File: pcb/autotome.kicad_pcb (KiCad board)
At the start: 2 copper layers, 61 parts, among them SW1 SW_PUSH, SW10 SW_PUSH, SW11 SW_PUSH, SW12 SW_PUSH, SW13 SW_PUSH, SW14 SW_PUSH, SW15 SW_PUSH, SW16 SW_PUSH, SW17 SW_PUSH, SW18 SW_PUSH, SW19 SW_PUSH, SW2 SW_PUSH, SW20 SW_PUSH, SW21 SW_PUSH, SW22 SW_PUSH, SW23 SW_PUSH, SW24 SW_PUSH, SW25 RotaryEncoder_Switch, SW27 SW_PUSH, SW28 SW_PUSH, SW29 SW_PUSH, SW3 SW_PUSH, SW30 SW_PUSH, SW31 SW_SPDT, SW4 SW_PUSH, SW5 SW_PUSH, SW6 SW_PUSH, SW7 SW_PUSH, SW8 SW_PUSH, SW9 SW_PUSH, U1 ProMicro

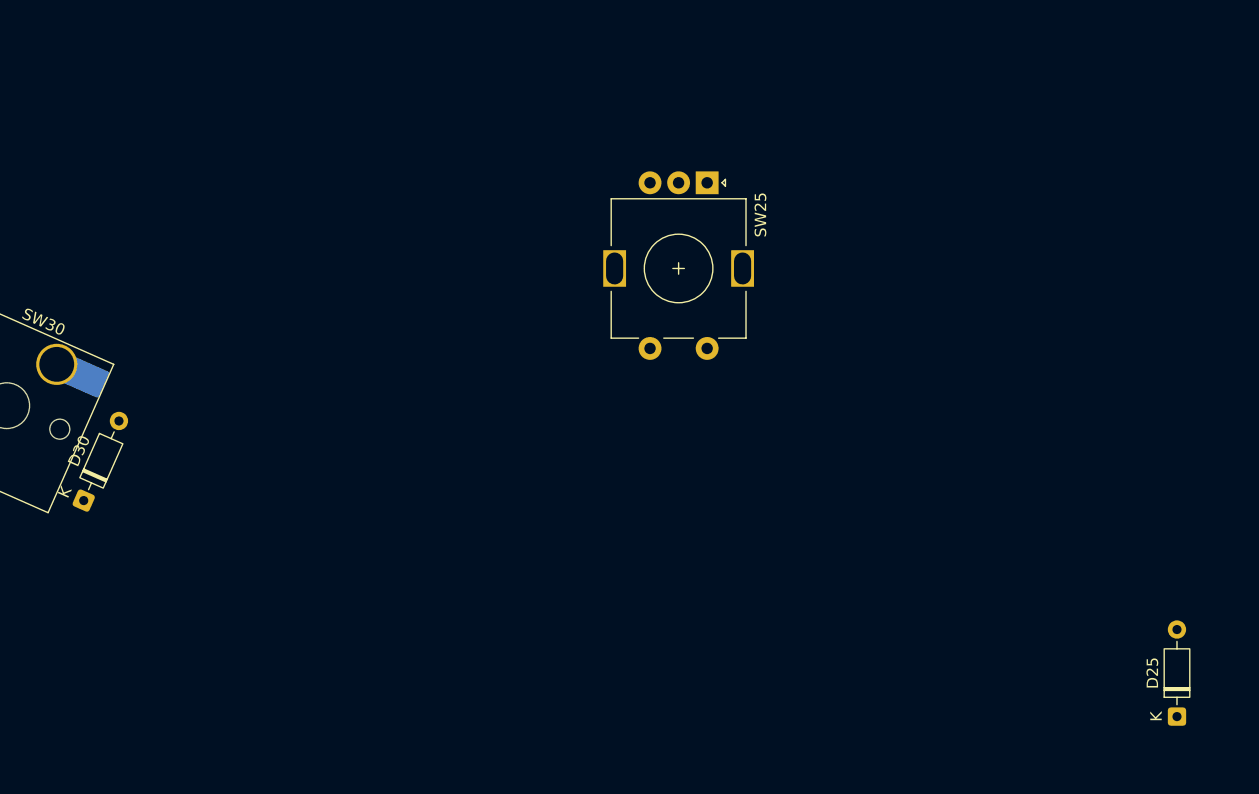
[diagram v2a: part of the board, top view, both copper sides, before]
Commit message: position rotary encoder and diode
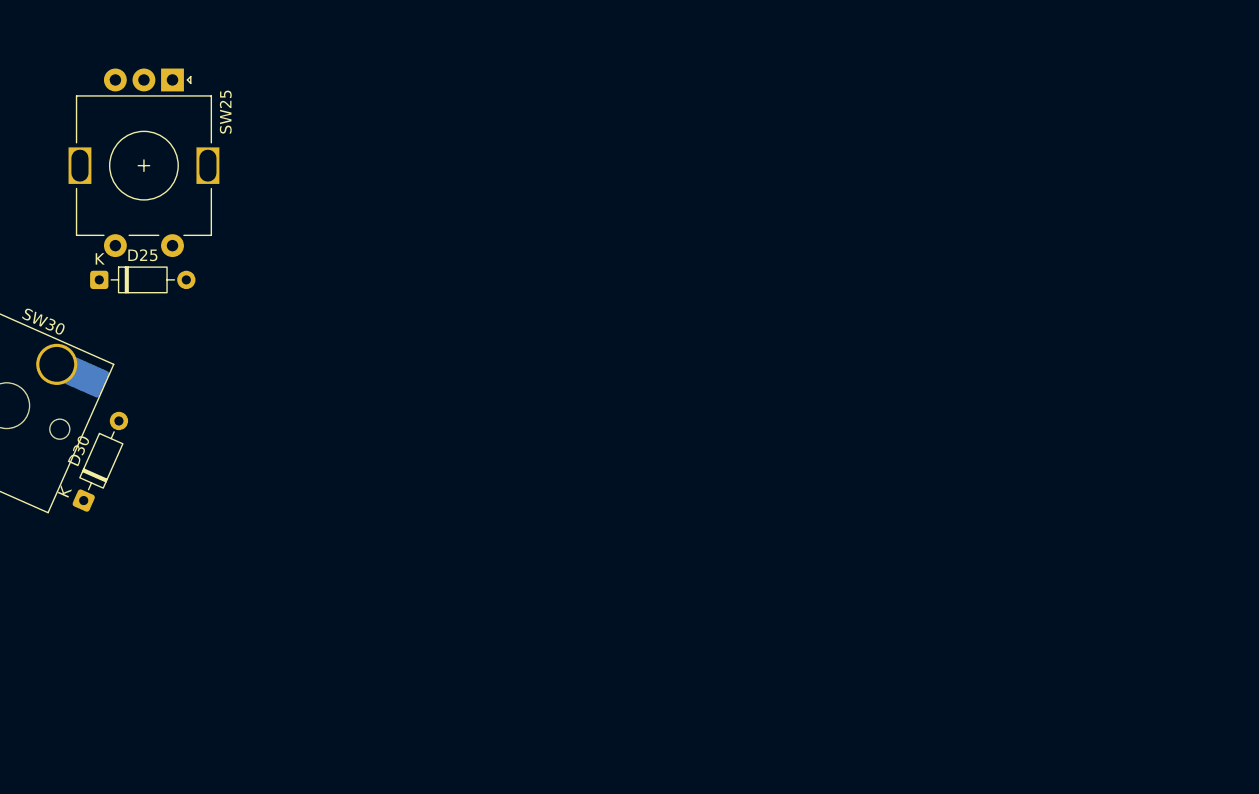
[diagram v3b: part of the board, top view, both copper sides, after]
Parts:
- moved D25 101.8 mm to (143.8, 123.7), turned to 0 degrees
- moved SW25 47.7 mm to (150.2, 106.2)
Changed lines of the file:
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@@
 	(footprint "Diode_THT:D_DO-35_SOD27_P7.62mm_Horizontal"
 		(layer "F.Cu")
-		(at 238.125 161.925 90)
+		(at 143.79 123.7)
 		(descr "Diode, DO-35_SOD27 series, Axial, Horizontal, pin pitch=7.62mm, length*diameter=4*2mm^2, http://www.diodes.com/_files/packages/DO-35.pdf")
 		(tags "Diode DO-35_SOD27 series Axial Horizontal pin pitch 7.62mm  length 4mm diameter 2mm")
 		(property "Reference" "D25"
-			(at 3.81 -2.12 90)
+			(at 3.81 -2.12 0)
 			(layer "F.SilkS")
 			(effects
@@
 		)
 		(property "Value" "1N4148"
-			(at 3.81 2.12 90)
+			(at 3.81 2.12 0)
 			(layer "F.Fab")
 			(effects
@@
 		)
 		(property "Datasheet" "https://assets.nexperia.com/documents/data-sheet/1N4148_1N4448.pdf"
-			(at 0 0 90)
+			(at 0 0 0)
 			(layer "F.Fab")
 			(hide yes)
@@
 		)
 		(property "Description" "100V 0.15A standard switching diode, DO-35"
-			(at 0 0 90)
+			(at 0 0 0)
 			(layer "F.Fab")
 			(hide yes)
@@
 		)
 		(property "KiLib_Generator" "diode/THT"
-			(at 0 0 90)
+			(at 0 0 0)
 			(layer "F.SilkS")
 			(hide yes)
@@
 		)
 		(property "Sim.Device" "D"
-			(at 0 0 90)
+			(at 0 0 0)
 			(unlocked yes)
 			(layer "F.Fab")
@@
 		)
 		(property "Sim.Pins" "1=K 2=A"
-			(at 0 0 90)
+			(at 0 0 0)
 			(unlocked yes)
 			(layer "F.Fab")
@@
 		(duplicate_pad_numbers_are_jumpers no)
 		(fp_line
+			(start 1.04 0)
+			(end 1.69 0)
+			(stroke
+				(width 0.12)
+				(type solid)
+			)
+			(layer "F.SilkS")
+		)
+		(fp_line
+			(start 2.29 -1.12)
+			(end 2.29 1.12)
+			(stroke
+				(width 0.12)
+				(type solid)
+			)
+			(layer "F.SilkS")
+		)
+		(fp_line
+			(start 2.41 -1.12)
+			(end 2.41 1.12)
+			(stroke
+				(width 0.12)
+				(type solid)
+			)
+			(layer "F.SilkS")
+		)
+		(fp_line
 			(start 2.53 -1.12)
 			(end 2.53 1.12)
@@
 		)
 		(fp_line
-			(start 2.41 -1.12)
-			(end 2.41 1.12)
-			(stroke
-				(width 0.12)
-				(type solid)
-			)
-			(layer "F.SilkS")
-		)
-		(fp_line
-			(start 2.29 -1.12)
-			(end 2.29 1.12)
-			(stroke
-				(width 0.12)
-				(type solid)
-			)
-			(layer "F.SilkS")
-		)
-		(fp_line
 			(start 6.58 0)
 			(end 5.93 0)
-			(stroke
-				(width 0.12)
-				(type solid)
-			)
-			(layer "F.SilkS")
-		)
-		(fp_line
-			(start 1.04 0)
-			(end 1.69 0)
 			(stroke
 				(width 0.12)
@@
 		)
 		(fp_line
+			(start 0 0)
+			(end 1.81 0)
+			(stroke
+				(width 0.1)
+				(type solid)
+			)
+			(layer "F.Fab")
+		)
+		(fp_line
+			(start 2.31 -1)
+			(end 2.31 1)
+			(stroke
+				(width 0.1)
+				(type solid)
+			)
+			(layer "F.Fab")
+		)
+		(fp_line
+			(start 2.41 -1)
+			(end 2.41 1)
+			(stroke
+				(width 0.1)
+				(type solid)
+			)
+			(layer "F.Fab")
+		)
+		(fp_line
 			(start 2.51 -1)
 			(end 2.51 1)
@@
 		)
 		(fp_line
-			(start 2.41 -1)
-			(end 2.41 1)
-			(stroke
-				(width 0.1)
-				(type solid)
-			)
-			(layer "F.Fab")
-		)
-		(fp_line
-			(start 2.31 -1)
-			(end 2.31 1)
-			(stroke
-				(width 0.1)
-				(type solid)
-			)
-			(layer "F.Fab")
-		)
-		(fp_line
 			(start 7.62 0)
 			(end 5.81 0)
-			(stroke
-				(width 0.1)
-				(type solid)
-			)
-			(layer "F.Fab")
-		)
-		(fp_line
-			(start 0 0)
-			(end 1.81 0)
 			(stroke
 				(width 0.1)
@@
 		)
 		(fp_text user "K"
-			(at 0 -1.8 90)
+			(at 0 -1.8 0)
 			(layer "F.SilkS")
 			(effects
@@
 		)
 		(fp_text user "K"
-			(at 0 -1.8 90)
+			(at 0 -1.8 0)
 			(layer "F.Fab")
 			(effects
@@
 		)
 		(fp_text user "${REFERENCE}"
-			(at 4.11 0 90)
+			(at 4.11 0 0)
 			(layer "F.Fab")
 			(effects
@@
 		)
 		(pad "1" thru_hole roundrect
-			(at 0 0 90)
+			(at 0 0)
 			(size 1.6 1.6)
 			(drill 0.8)
@@
 		)
 		(pad "2" thru_hole circle
-			(at 7.62 0 90)
+			(at 7.62 0)
 			(size 1.6 1.6)
 			(drill 0.8)
@@
 	(footprint "autotome_library:RotaryEncoder_Alps_EC11E-Switch_Vertical_H20mm"
 		(layer "F.Cu")
-		(at 197 115.2 -90)
+		(at 150.2 106.2 -90)
 		(descr "Alps rotary encoder, EC11E... with switch, vertical shaft, http://www.alps.com/prod/info/E/HTML/Encoder/Incremental/EC11/EC11E15204A3.html")
 		(tags "rotary encoder")

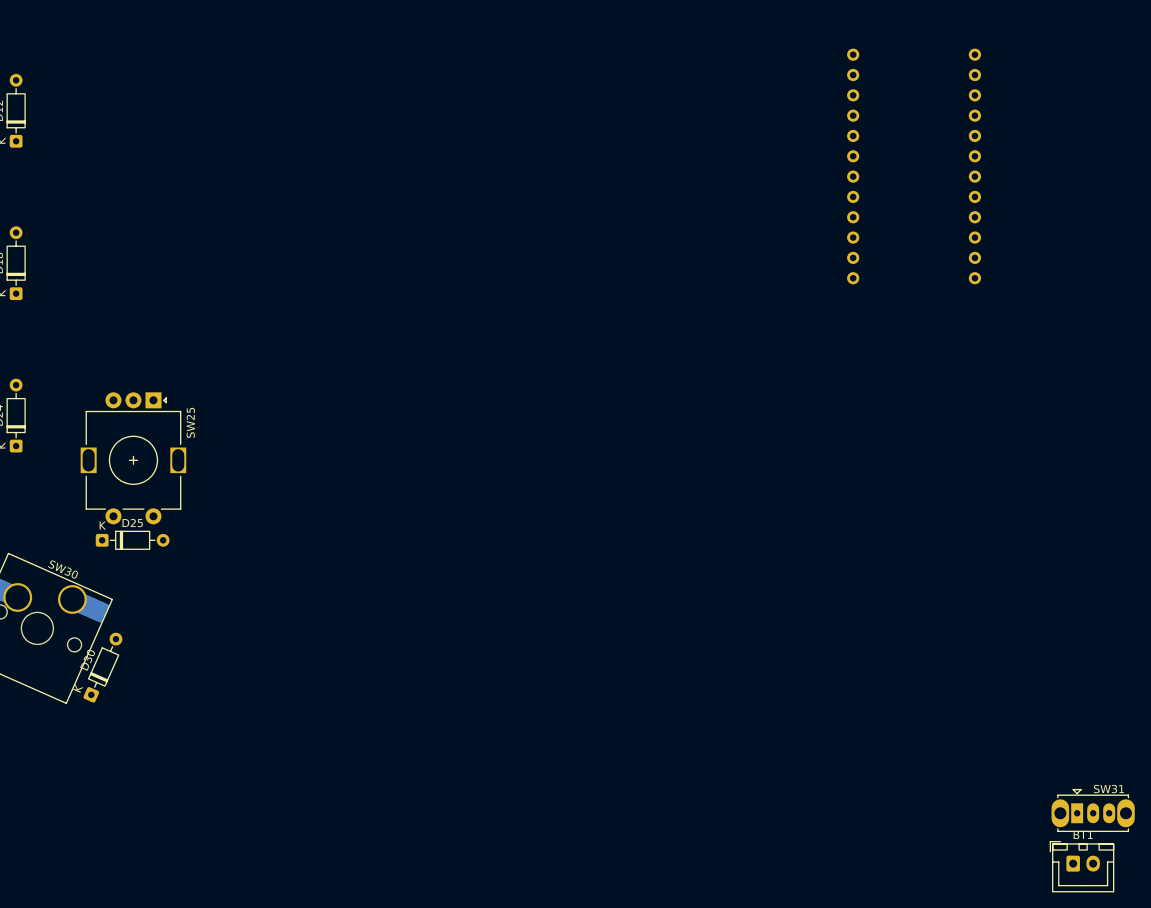
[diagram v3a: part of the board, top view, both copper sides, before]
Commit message: position nicenano, on/off switch, jst
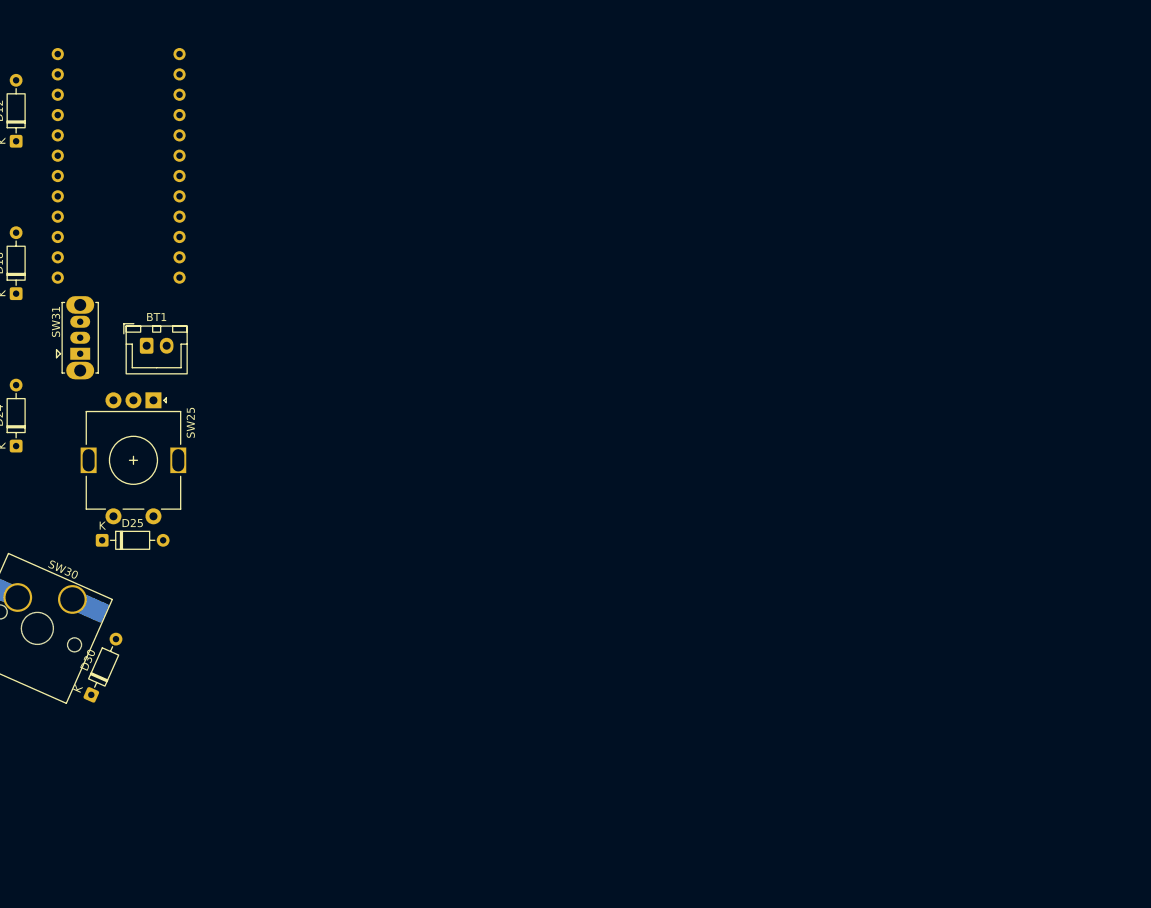
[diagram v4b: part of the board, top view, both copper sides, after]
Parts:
- moved SW31 137.2 mm to (141.0, 100.4), turned to 90 degrees
- moved BT1 132.7 mm to (149.3, 99.4)
- moved U1 99.4 mm to (145.8, 77.4)
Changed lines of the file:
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@@
 	(footprint "Connector_JST:JST_XH_B2B-XH-A_1x02_P2.50mm_Vertical"
 		(layer "F.Cu")
-		(at 265.1625 164.115)
+		(at 149.35 99.378)
 		(descr "JST XH series connector, B2B-XH-A (http://www.jst-mfg.com/product/pdf/eng/eXH.pdf)")
 		(tags "connector JST XH vertical")
@@
 	(footprint "Button_Switch_THT:SW_Slide_SPDT_Straight_CK_OS102011MS2Q"
 		(layer "F.Cu")
-		(at 265.6625 157.82)
+		(at 141.0414 100.378 90)
 		(descr "CuK miniature slide switch, OS series, SPDT, https://www.ckswitches.com/media/1428/os.pdf")
 		(tags "switch SPDT")
 		(property "Reference" "SW31"
-			(at 3.99 -2.99 0)
+			(at 3.99 -2.99 90)
 			(layer "F.SilkS")
 			(effects
@@
 		)
 		(property "Value" "SW_SPDT"
-			(at 2 3 0)
+			(at 2 3 90)
 			(layer "F.Fab")
 			(effects
@@
 		)
 		(property "Datasheet" ""
-			(at 0 0 0)
+			(at 0 0 90)
 			(unlocked yes)
 			(layer "F.Fab")
@@
 		)
 		(property "Description" "Switch, single pole double throw"
-			(at 0 0 0)
+			(at 0 0 90)
 			(unlocked yes)
 			(layer "F.Fab")
@@
 		(duplicate_pad_numbers_are_jumpers no)
 		(fp_line
-			(start -2.41 -2.26)
-			(end 6.41 -2.26)
+			(start 0.5 -2.96)
+			(end -0.5 -2.96)
 			(stroke
 				(width 0.12)
@@
 		)
 		(fp_line
-			(start -2.41 -1.95)
-			(end -2.41 -2.26)
+			(start -0.5 -2.96)
+			(end 0 -2.46)
 			(stroke
 				(width 0.12)
@@
 		)
 		(fp_line
-			(start -2.41 2.26)
-			(end -2.41 1.95)
+			(start 0 -2.46)
+			(end 0.5 -2.96)
 			(stroke
 				(width 0.12)
@@
 		)
 		(fp_line
-			(start -0.5 -2.96)
-			(end 0 -2.46)
+			(start 6.41 -2.26)
+			(end 6.41 -1.95)
 			(stroke
 				(width 0.12)
@@
 		)
 		(fp_line
-			(start 0 -2.46)
-			(end 0.5 -2.96)
+			(start -2.41 -2.26)
+			(end 6.41 -2.26)
 			(stroke
 				(width 0.12)
@@
 		)
 		(fp_line
-			(start 0.5 -2.96)
-			(end -0.5 -2.96)
+			(start -2.41 -1.95)
+			(end -2.41 -2.26)
 			(stroke
 				(width 0.12)
@@
 		)
 		(fp_line
-			(start 6.41 -2.26)
-			(end 6.41 -1.95)
+			(start 6.41 2.26)
+			(end 6.41 1.95)
 			(stroke
 				(width 0.12)
@@
 		)
 		(fp_line
-			(start 6.41 2.26)
-			(end 6.41 1.95)
+			(start -2.41 2.26)
+			(end -2.41 1.95)
 			(stroke
 				(width 0.12)
@@
 		)
 		(fp_line
-			(start -3.45 -2.4)
-			(end 7.45 -2.4)
+			(start 7.45 -2.4)
+			(end 7.45 2.4)
 			(stroke
 				(width 0.05)
@@
 		)
 		(fp_line
-			(start -3.45 2.4)
-			(end -3.45 -2.4)
+			(start -3.45 -2.4)
+			(end 7.45 -2.4)
 			(stroke
 				(width 0.05)
@@
 		)
 		(fp_line
-			(start 7.45 -2.4)
-			(end 7.45 2.4)
+			(start 7.45 2.4)
+			(end -3.45 2.4)
 			(stroke
 				(width 0.05)
@@
 		)
 		(fp_line
-			(start 7.45 2.4)
-			(end -3.45 2.4)
+			(start -3.45 2.4)
+			(end -3.45 -2.4)
 			(stroke
 				(width 0.05)
@@
 		)
 		(fp_line
-			(start -2.3 -2.15)
-			(end -0.5 -2.15)
+			(start 6.3 -2.15)
+			(end 6.3 2.15)
 			(stroke
 				(width 0.1)
@@
 		)
 		(fp_line
-			(start -2.3 2.15)
-			(end -2.3 -2.15)
+			(start 0.5 -2.15)
+			(end 6.3 -2.15)
 			(stroke
 				(width 0.1)
@@
 		)
 		(fp_line
-			(start 0 -1.65)
-			(end 0.5 -2.15)
+			(start -2.3 -2.15)
+			(end -0.5 -2.15)
 			(stroke
 				(width 0.1)
@@
 		)
 		(fp_line
-			(start 0 -1)
-			(end 0 1)
+			(start 0 -1.65)
+			(end 0.5 -2.15)
 			(stroke
 				(width 0.1)
@@
 		)
 		(fp_line
-			(start 0 -1)
-			(end 4 -1)
+			(start 4 -1)
+			(end 4 1)
 			(stroke
 				(width 0.1)
@@
 		)
 		(fp_line
-			(start 0 1)
-			(end 4 1)
+			(start 2 -1)
+			(end 2 1)
 			(stroke
 				(width 0.1)
@@
 		)
 		(fp_line
-			(start 0.5 -2.15)
-			(end 6.3 -2.15)
+			(start 1.34 -1)
+			(end 1.34 1)
 			(stroke
 				(width 0.1)
@@
 		)
 		(fp_line
-			(start 1.34 -1)
-			(end 1.34 1)
+			(start 0 -1)
+			(end 4 -1)
 			(stroke
 				(width 0.1)
@@
 		)
 		(fp_line
-			(start 2 -1)
-			(end 2 1)
+			(start 0 -1)
+			(end 0 1)
 			(stroke
 				(width 0.1)
@@
 		)
 		(fp_line
-			(start 4 -1)
+			(start 0 1)
 			(end 4 1)
 			(stroke
@@
 		)
 		(fp_line
-			(start 6.3 -2.15)
-			(end 6.3 2.15)
+			(start 6.3 2.15)
+			(end -2.3 2.15)
 			(stroke
 				(width 0.1)
@@
 		)
 		(fp_line
-			(start 6.3 2.15)
-			(end -2.3 2.15)
+			(start -2.3 2.15)
+			(end -2.3 -2.15)
 			(stroke
 				(width 0.1)
@@
 		)
 		(fp_text user "${REFERENCE}"
-			(at 3.99 -2.99 0)
+			(at 3.99 -2.99 90)
 			(layer "F.Fab")
 			(effects
@@
 		)
 		(pad "" thru_hole oval
-			(at -2.1 0)
+			(at -2.1 0 90)
 			(size 2.2 3.5)
 			(drill 1.5)
@@
 		)
 		(pad "" thru_hole oval
-			(at 6.1 0)
+			(at 6.1 0 90)
 			(size 2.2 3.5)
 			(drill 1.5)
@@
 		)
 		(pad "1" thru_hole rect
-			(at 0 0)
+			(at 0 0 90)
 			(size 1.5 2.5)
 			(drill 0.8)
@@
 		)
 		(pad "2" thru_hole oval
-			(at 2 0)
+			(at 2 0 90)
 			(size 1.5 2.5)
 			(drill 0.8)
@@
 		)
 		(pad "3" thru_hole oval
-			(at 4 0)
+			(at 4 0 90)
 			(size 1.5 2.5)
 			(drill 0.8)
@@
 	(footprint "autotome_library:NiceNano"
 		(layer "B.Cu")
-		(at 245.275 77.475 180)
+		(at 145.85 77.4 180)
 		(property "Reference" "U1"
 			(at 0 5 90)
